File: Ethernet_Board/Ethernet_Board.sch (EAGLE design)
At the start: 36 parts, among them J1 22-05-7028-02, J2 22-05-7068-06, J3 22-05-7068-06, P1 RB1-125BAG1A, T1 EXMACHINA-LOGO-NAME, U1 DP83848JSQ/NOPB, X1 ASE_50

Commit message: Update components names and value placement
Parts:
- C1: MPN (none) -> F931A475MAA; OC_NEWARK (none) -> 58R3271
- C10, C11, C12, C2, C3, C5, C6, C7, C9: MPN (none) -> MC0603B104K250CT; OC_NEWARK (none) -> 06R4925
- C4, C8: MPN (none) -> F931A106MAA; OC_NEWARK (none) -> 58R3260
- D1: OC_NEWARK (none) -> 06X0873
- H1, H2, H3, H4, JP1, JP2, JP3, JP4, P1, T1: OC_NEWARK (none) -> unknown
- J1: MPN (none) -> 22-05-7028; OC_NEWARK (none) -> 25M1728
- J2, J3: MPN (none) -> 22-05-7068; OC_NEWARK (none) -> 25M1733
- R1, R2: MPN (none) -> MCMR06X2200FTL; OC_NEWARK (none) -> 86T3577
- R3, R4, R5, R6: MPN (none) -> MCMR06X49R9FTL; OC_NEWARK (none) -> 86T3659
- R7: MPN (none) -> MCMR06X4701FTL; OC_NEWARK (none) -> 86T3649
- R8: MPN (none) -> MCMR06X2201FTL; OC_NEWARK (none) -> 86T3578
- U1: MPN (none) -> DP83848JSQ/NOPB; OC_NEWARK (none) -> 96W2841
- X1: MPN (none) -> ASE-50.000MHZ-LC-T; OC_NEWARK (none) -> 84R2105

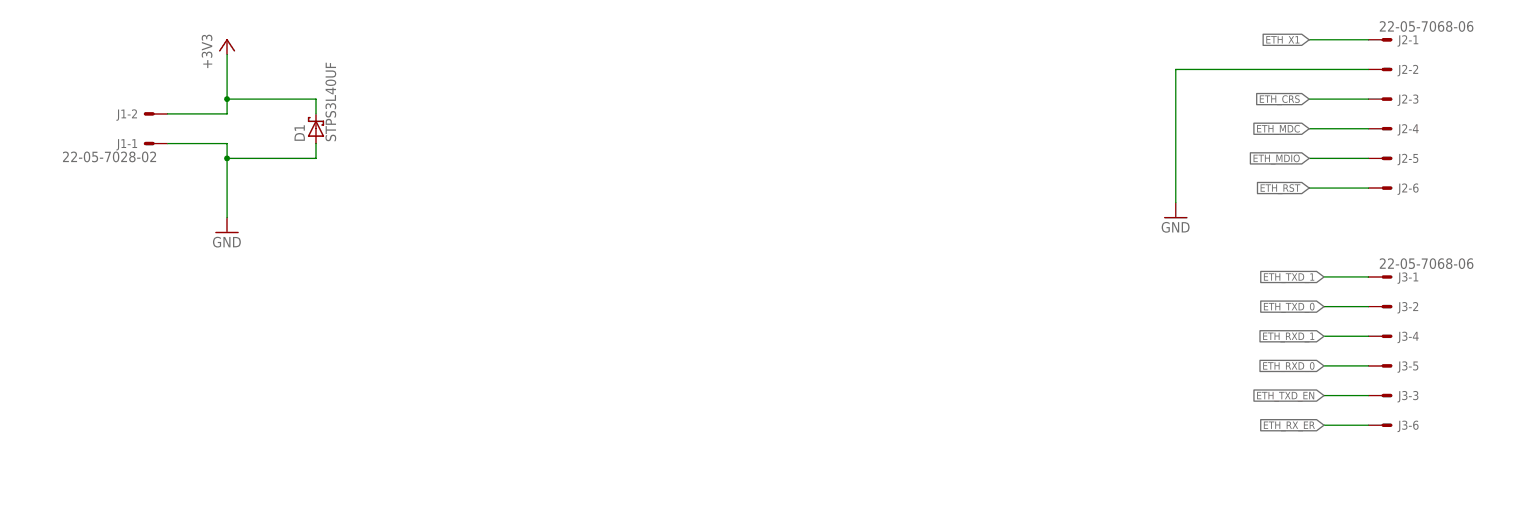
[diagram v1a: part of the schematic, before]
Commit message: Replace output connector and generate gerber files
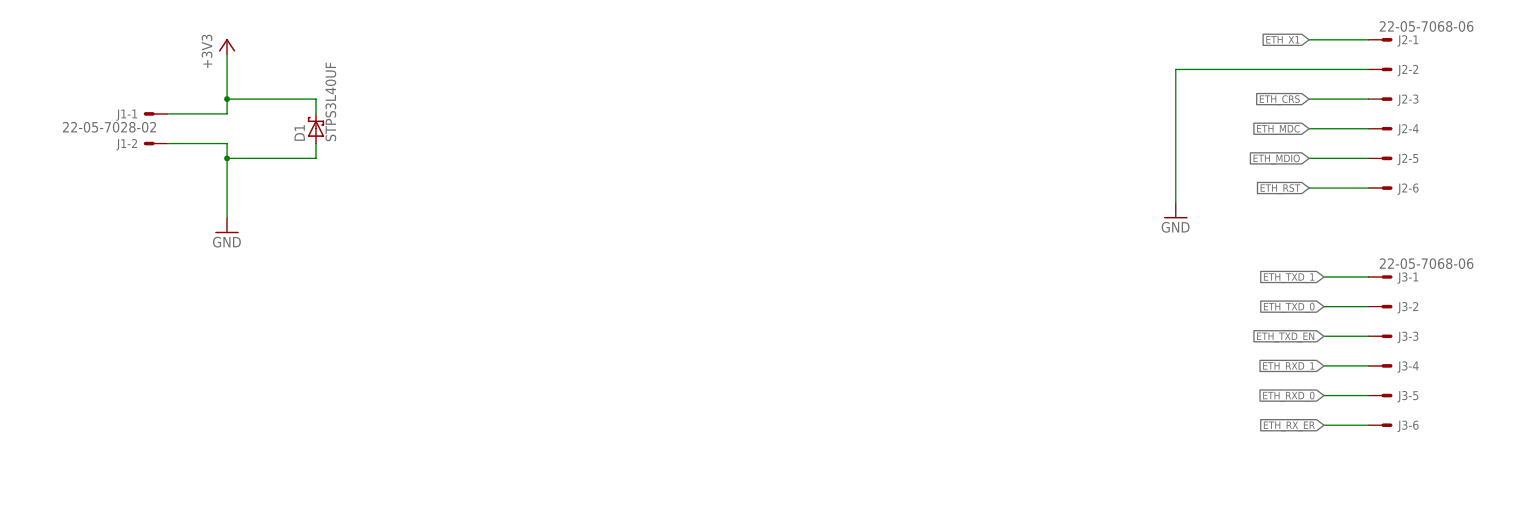
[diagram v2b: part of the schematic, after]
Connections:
- net +3V3: now also J1-1.S; no longer J1-2.S
- net GND: now also J1-2.S; no longer J1-1.S
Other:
- moved on the sheet: J1-1, J1-2, J3-3, J3-4, J3-5
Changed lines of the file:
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@@
 <attribute name="MPN" x="360.68" y="208.28" size="1.778" layer="96" display="off"/>
 </instance>
-<instance part="J1" gate="-1" x="27.94" y="76.2" rot="R180"/>
-<instance part="J1" gate="-2" x="27.94" y="81.28" rot="R180"/>
+<instance part="J1" gate="-1" x="27.94" y="81.28" rot="R180"/>
+<instance part="J1" gate="-2" x="27.94" y="76.2" rot="R180"/>
 <instance part="+3V31" gate="G$1" x="40.64" y="93.98"/>
 <instance part="GND1" gate="1" x="40.64" y="60.96"/>
@@
 <instance part="J3" gate="-1" x="238.76" y="53.34"/>
 <instance part="J3" gate="-2" x="238.76" y="48.26"/>
-<instance part="J3" gate="-4" x="238.76" y="43.18"/>
-<instance part="J3" gate="-5" x="238.76" y="38.1"/>
-<instance part="J3" gate="-3" x="238.76" y="33.02"/>
+<instance part="J3" gate="-4" x="238.76" y="38.1"/>
+<instance part="J3" gate="-5" x="238.76" y="33.02"/>
+<instance part="J3" gate="-3" x="238.76" y="43.18"/>
 <instance part="J3" gate="-6" x="238.76" y="27.94"/>
 <instance part="GND10" gate="1" x="203.2" y="63.5"/>
@@
 </segment>
 <segment>
-<pinref part="J1" gate="-1" pin="S"/>
 <pinref part="GND1" gate="1" pin="GND"/>
-<wire x1="30.48" y1="76.2" x2="40.64" y2="76.2" width="0.1524" layer="91"/>
 <wire x1="40.64" y1="76.2" x2="40.64" y2="73.66" width="0.1524" layer="91"/>
 <pinref part="D1" gate="A" pin="A"/>
@@
 <wire x1="55.88" y1="73.66" x2="40.64" y2="73.66" width="0.1524" layer="91"/>
 <junction x="40.64" y="73.66"/>
+<pinref part="J1" gate="-2" pin="S"/>
+<wire x1="30.48" y1="76.2" x2="40.64" y2="76.2" width="0.1524" layer="91"/>
 </segment>
 <segment>
@@
 </segment>
 <segment>
-<pinref part="J1" gate="-2" pin="S"/>
 <pinref part="+3V31" gate="G$1" pin="+3V3"/>
-<wire x1="30.48" y1="81.28" x2="40.64" y2="81.28" width="0.1524" layer="91"/>
 <wire x1="40.64" y1="81.28" x2="40.64" y2="83.82" width="0.1524" layer="91"/>
 <pinref part="D1" gate="A" pin="C"/>
@@
 <wire x1="55.88" y1="83.82" x2="40.64" y2="83.82" width="0.1524" layer="91"/>
 <junction x="40.64" y="83.82"/>
+<pinref part="J1" gate="-1" pin="S"/>
+<wire x1="30.48" y1="81.28" x2="40.64" y2="81.28" width="0.1524" layer="91"/>
 </segment>
 </net>
@@
 </segment>
 <segment>
-<wire x1="236.22" y1="33.02" x2="228.6" y2="33.02" width="0.1524" layer="91"/>
-<label x="228.6" y="33.02" size="1.27" layer="95" rot="R180" xref="yes"/>
+<wire x1="236.22" y1="43.18" x2="228.6" y2="43.18" width="0.1524" layer="91"/>
+<label x="228.6" y="43.18" size="1.27" layer="95" rot="R180" xref="yes"/>
 <pinref part="J3" gate="-3" pin="S"/>
 </segment>
@@
 </segment>
 <segment>
-<wire x1="236.22" y1="43.18" x2="228.6" y2="43.18" width="0.1524" layer="91"/>
-<label x="228.6" y="43.18" size="1.27" layer="95" rot="R180" xref="yes"/>
+<wire x1="236.22" y1="38.1" x2="228.6" y2="38.1" width="0.1524" layer="91"/>
+<label x="228.6" y="38.1" size="1.27" layer="95" rot="R180" xref="yes"/>
 <pinref part="J3" gate="-4" pin="S"/>
 </segment>
@@
 </segment>
 <segment>
-<wire x1="236.22" y1="38.1" x2="228.6" y2="38.1" width="0.1524" layer="91"/>
-<label x="228.6" y="38.1" size="1.27" layer="95" rot="R180" xref="yes"/>
+<wire x1="236.22" y1="33.02" x2="228.6" y2="33.02" width="0.1524" layer="91"/>
+<label x="228.6" y="33.02" size="1.27" layer="95" rot="R180" xref="yes"/>
 <pinref part="J3" gate="-5" pin="S"/>
 </segment>
